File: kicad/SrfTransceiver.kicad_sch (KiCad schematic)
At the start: 22 parts

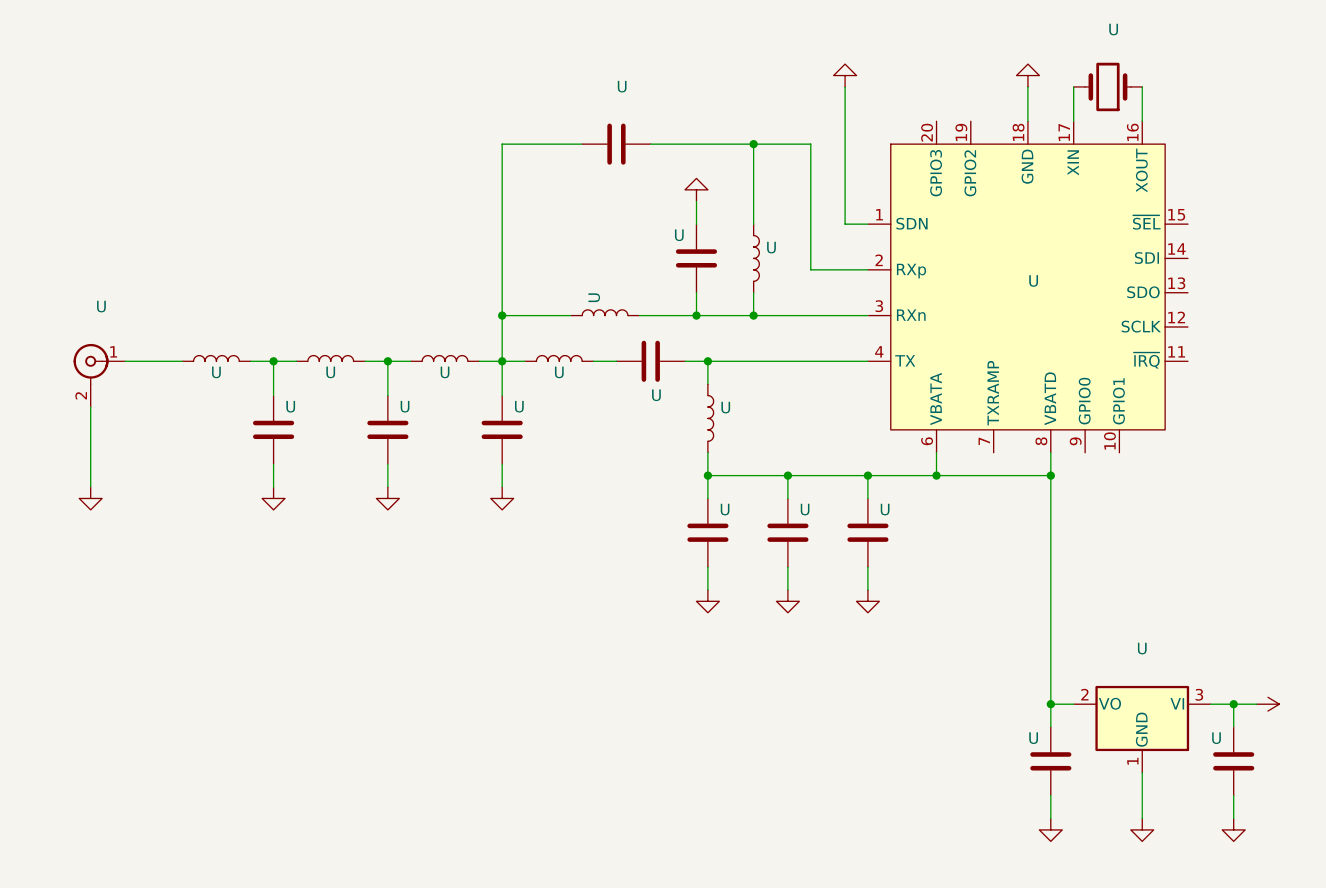
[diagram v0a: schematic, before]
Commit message: Adding PIB USB BRIDGE UML state diagrams - WIP
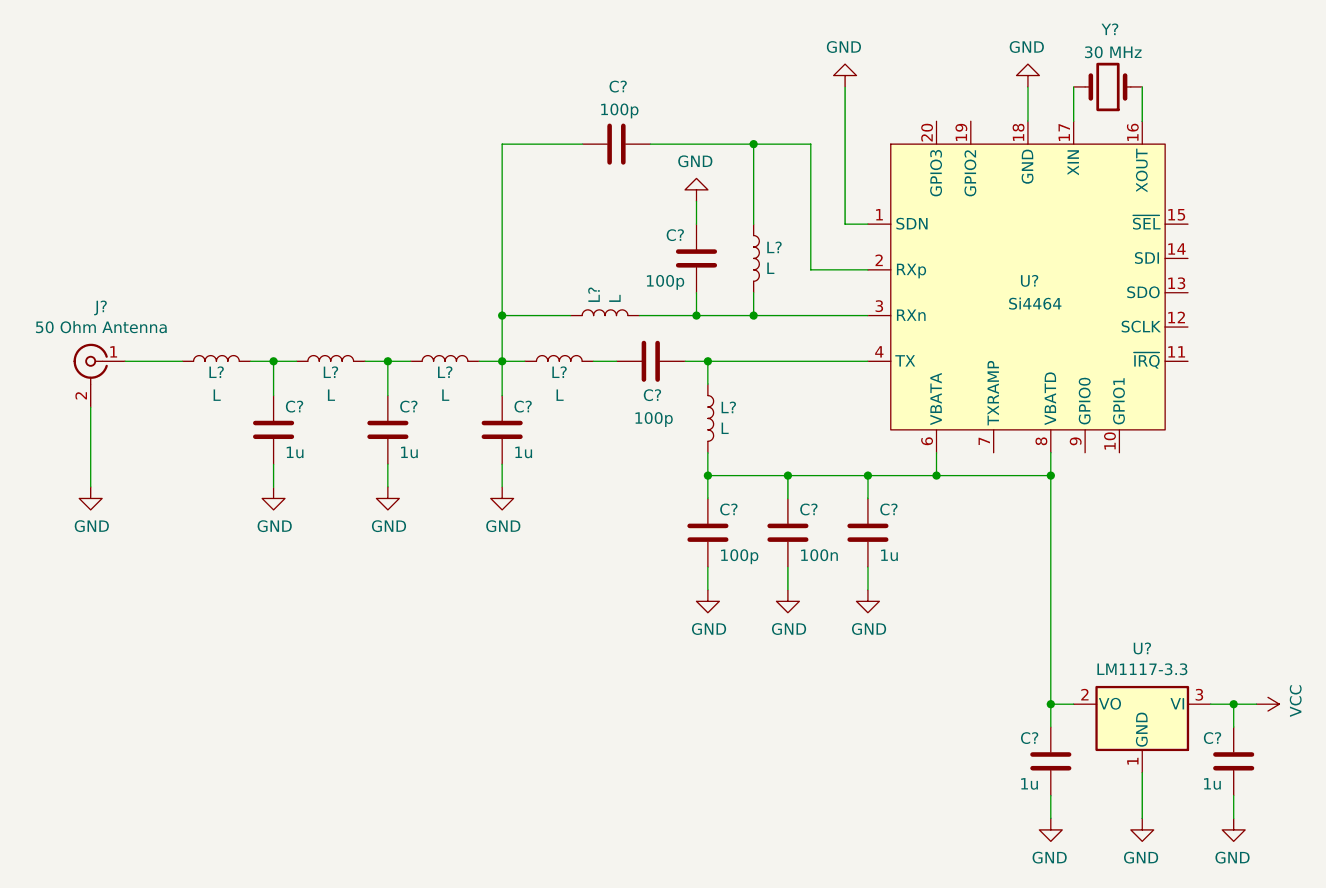
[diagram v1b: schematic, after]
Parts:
- C? (x4): renamed from U; value (none) -> 100p; symbol device:C -> RCTX-rescue:C-device
- C?: renamed from U; value (none) -> 100n; symbol device:C -> RCTX-rescue:C-device
- C? (x6): renamed from U; value (none) -> 1u; symbol device:C -> RCTX-rescue:C-device
- J?: renamed from U; value (none) -> 50 Ohm Antenna; symbol conn:Conn_Coaxial -> RCTX-rescue:Conn_Coaxial-conn
- L? (x7): renamed from U; value (none) -> L; symbol device:L -> RCTX-rescue:L-device
- U?: renamed from U; value (none) -> Si4464; footprint (none) -> Package_DFN_QFN:QFN-20-1EP_4x4mm_P0.5mm_EP2.6x2.6mm_ThermalVias; symbol RF:Si4464 -> RCTX-rescue:Si4464-RF
- U?: renamed from U; value (none) -> LM1117-3.3; symbol regul:LM1117-3.3 -> RCTX-rescue:LM1117-3.3-regul
- Y?: renamed from U; value (none) -> 30 MHz; symbol device:Crystal -> RCTX-rescue:Crystal-device
